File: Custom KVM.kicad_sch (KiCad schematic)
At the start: 2 parts, among them U1 TS3DV642A0RUAR, U2 TS3DV642A0RUAR

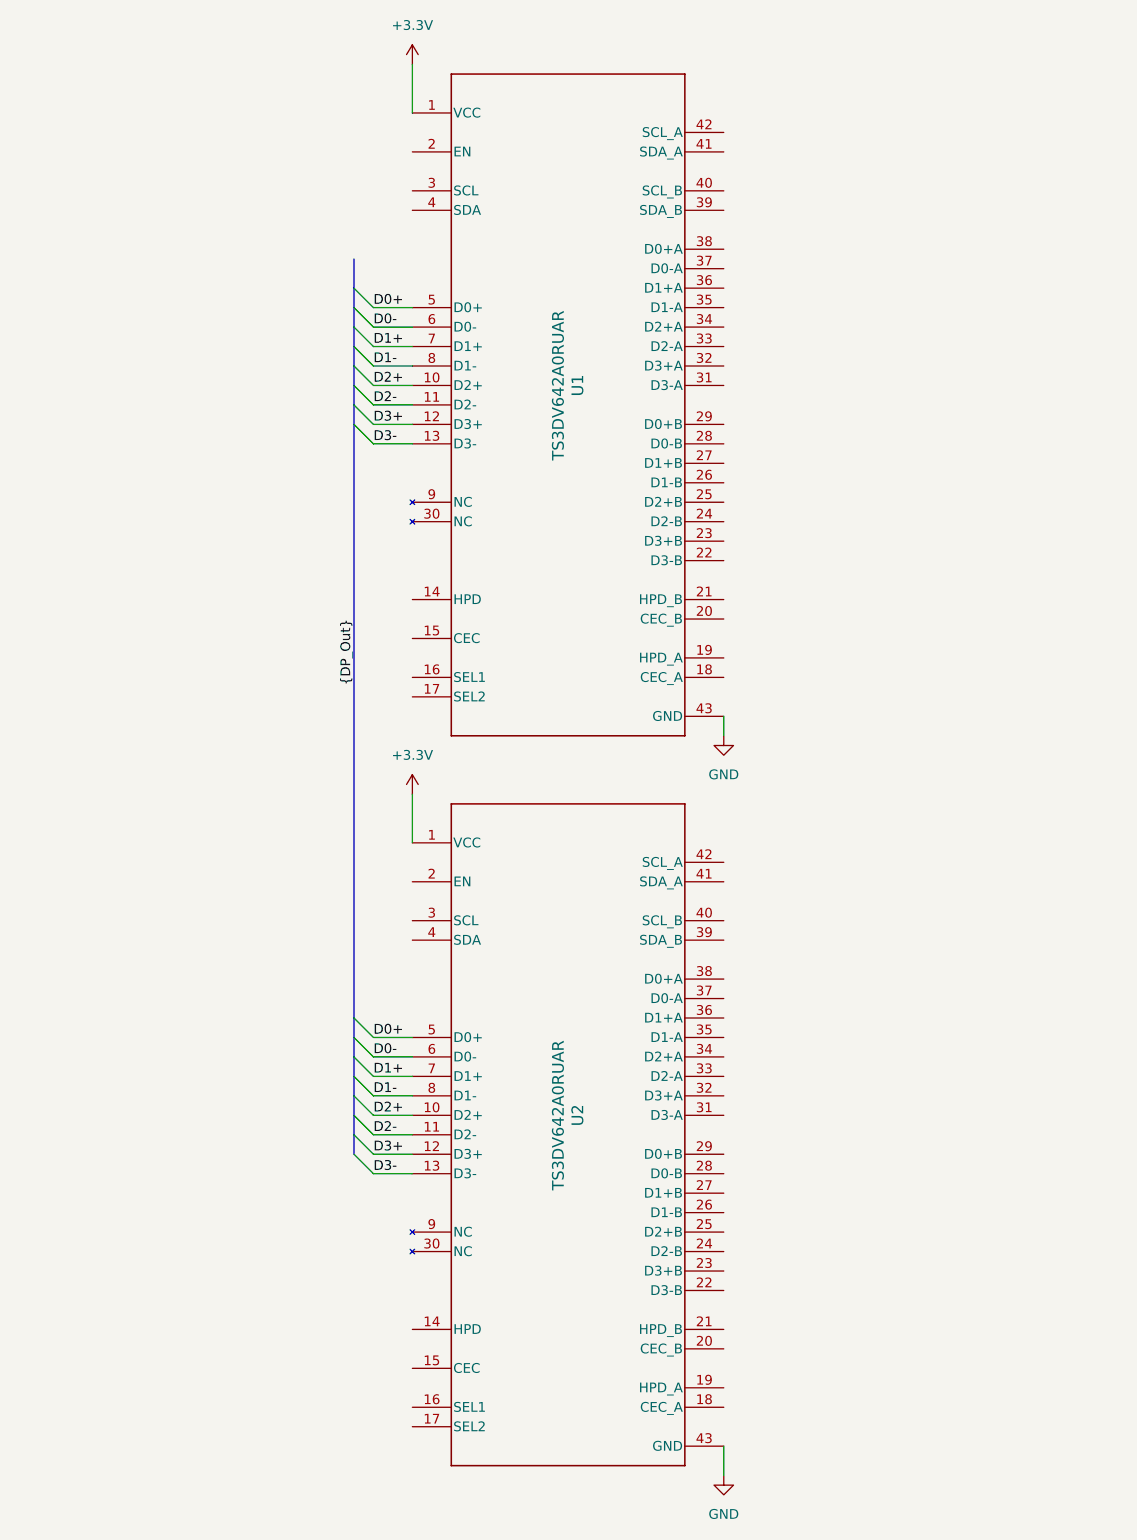
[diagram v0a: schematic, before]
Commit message: Add counter an CE circuit
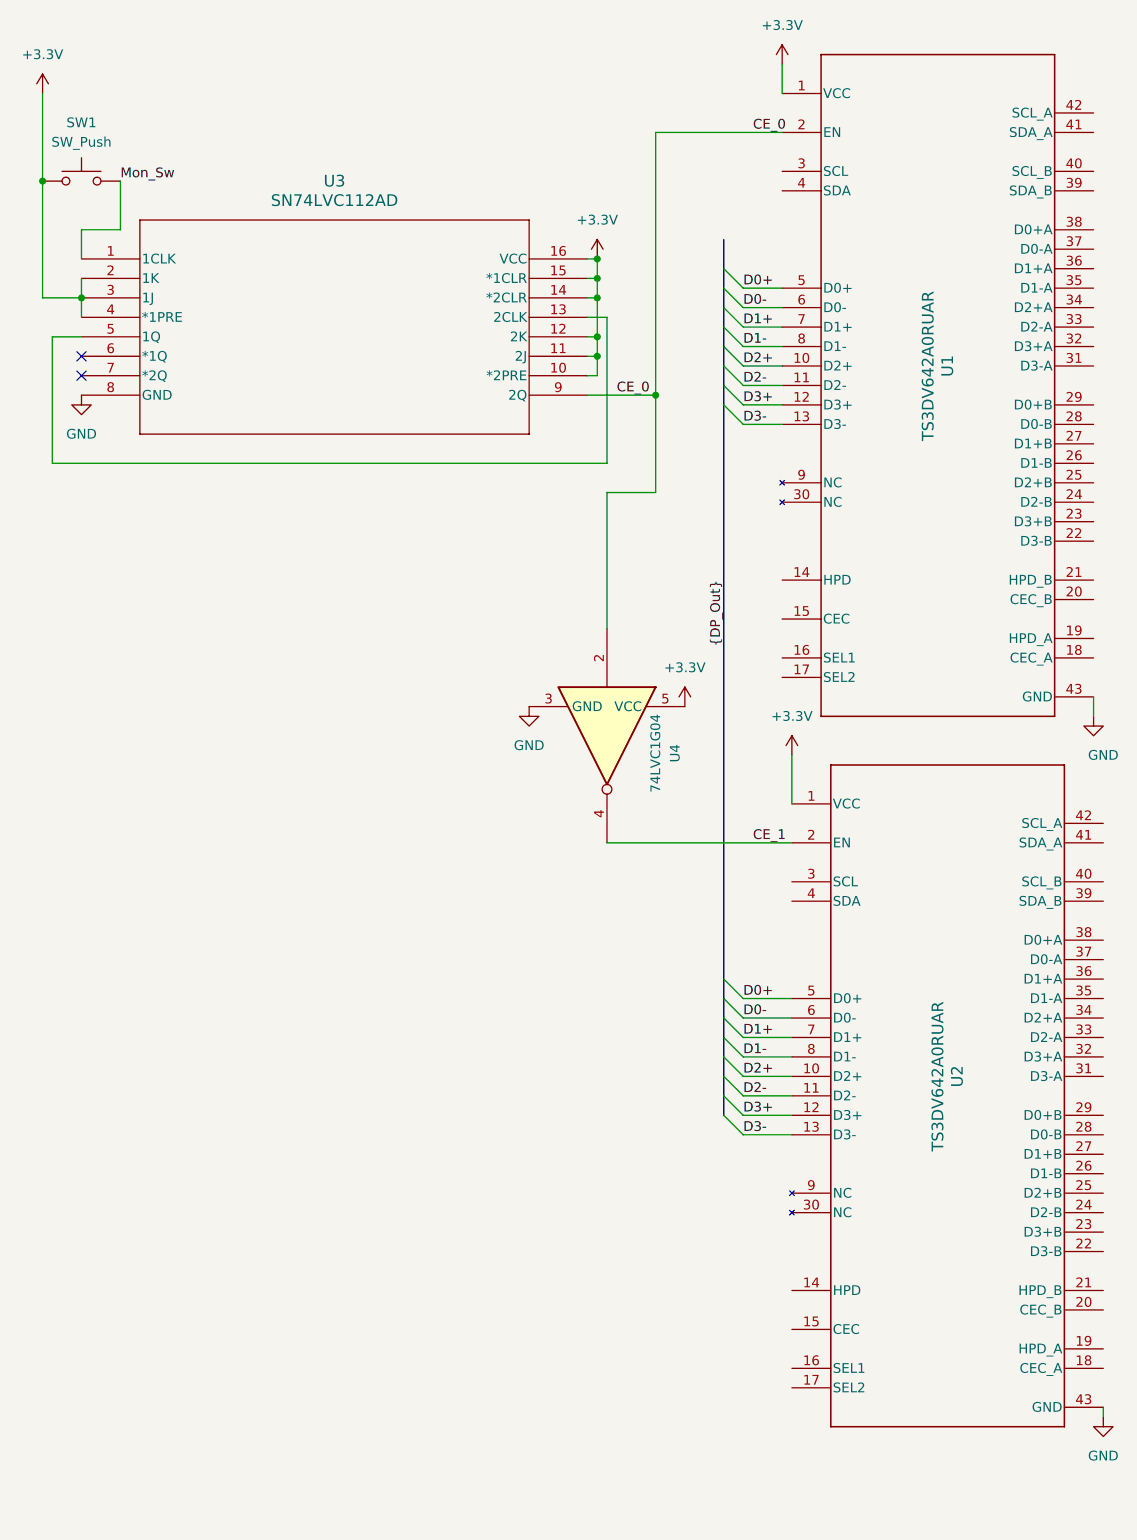
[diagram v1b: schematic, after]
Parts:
- added SW1: SW_Push, symbol Switch:SW_Push
- added U3: SN74LVC112AD, D16, symbol SN74LVC112A:SN74LVC112AD
- added U4: 74LVC1G04, symbol 74xGxx:74LVC1G04
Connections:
- net +3.3V: now also SW1.1, U3.10 (*2PRE), U3.11 (2J), U3.12 (2K), U3.14 (*2CLR), U3.15 (*1CLR), U3.16 (VCC), U3.2 (1K), U3.3 (1J), U3.4 (*1PRE), U4.5 (VCC)
- net GND: now also U3.8 (GND), U4.3 (GND)
- net CE_0: now reaches U1.2 (EN)
- net CE_0: now also U3.9 (2Q), U4.2
- net CE_1: now reaches U2.2 (EN)
- net CE_1: now also U4.4
- new net: U3.13 (2CLK), U3.5 (1Q)
- new net Mon_Sw: SW1.2, U3.1 (1CLK)
- no-connect marks 0 -> 2
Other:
- moved on the sheet: U1, U2

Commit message: Move counter and inverters to sub-sheet
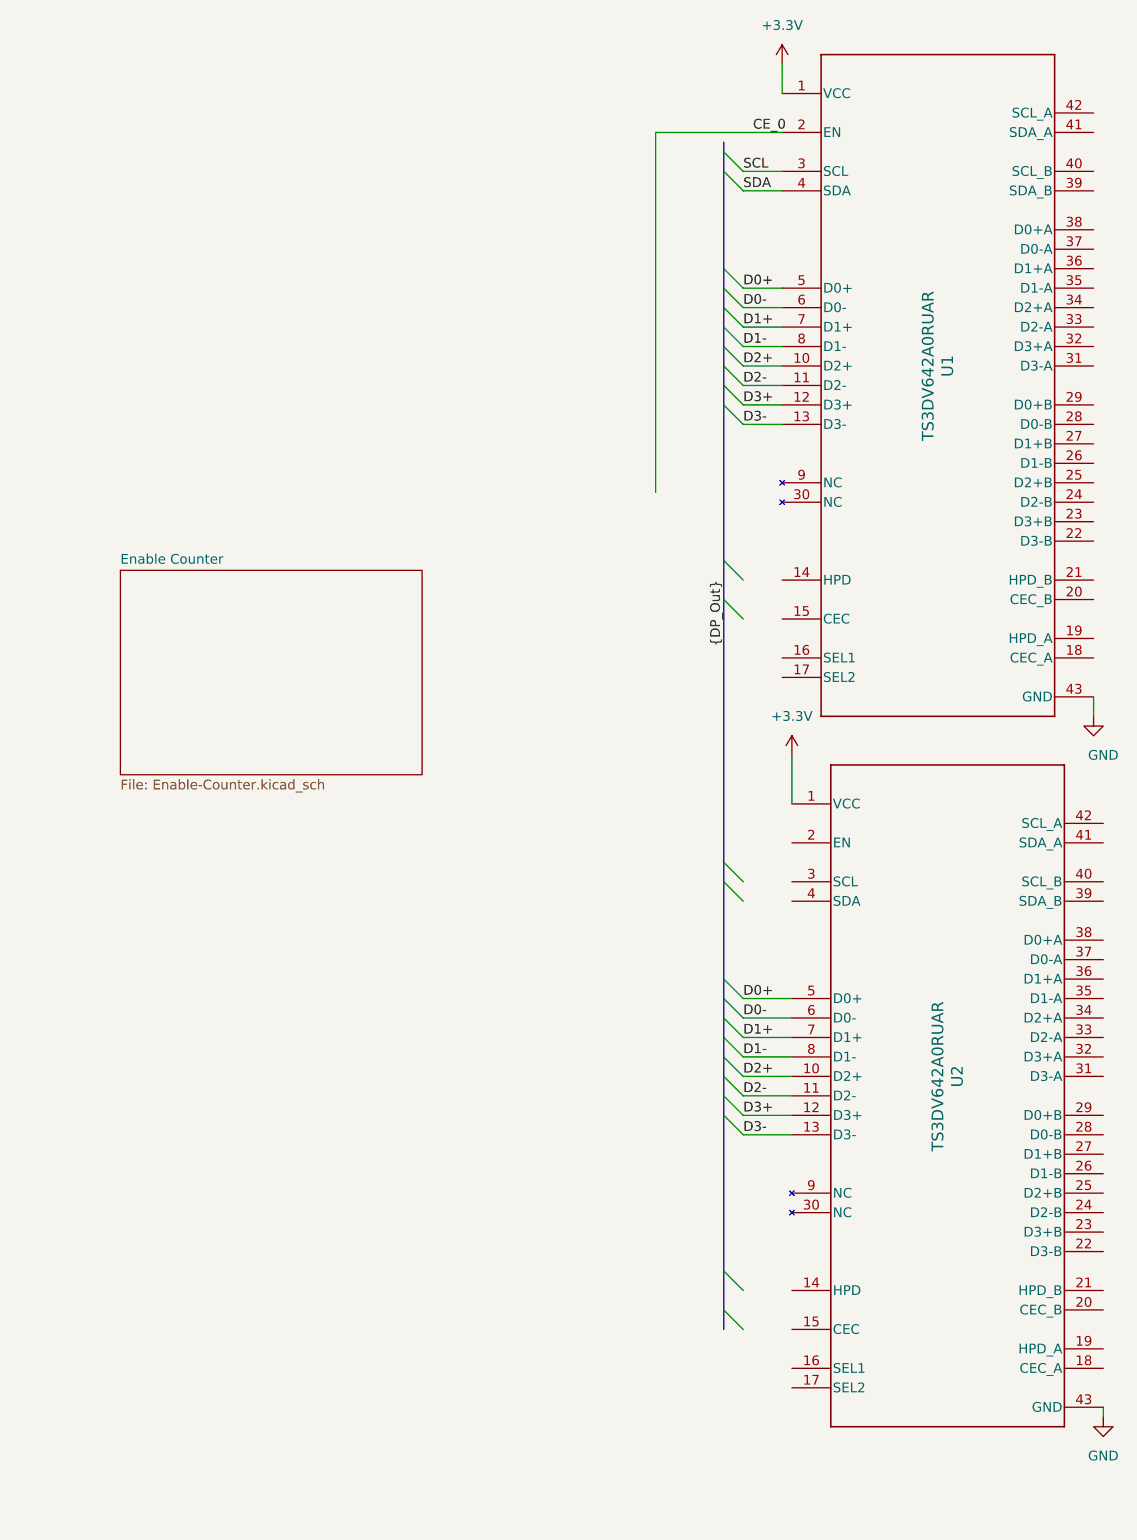
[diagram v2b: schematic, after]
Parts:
- removed SW1: SW_Push, symbol Switch:SW_Push
- removed U3: SN74LVC112AD, D16, symbol SN74LVC112A:SN74LVC112AD
- removed U4: 74LVC1G04, symbol 74xGxx:74LVC1G04
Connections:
- net SCL: now reaches U1.3 (SCL)
- net SDA: now reaches U1.4 (SDA)
- net CE_1: no longer names the net of U2.2 (EN)
- no-connect marks 2 -> 0
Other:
- added sheet Enable Counter (Enable-Counter.kicad_sch)

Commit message: Added mDP connector
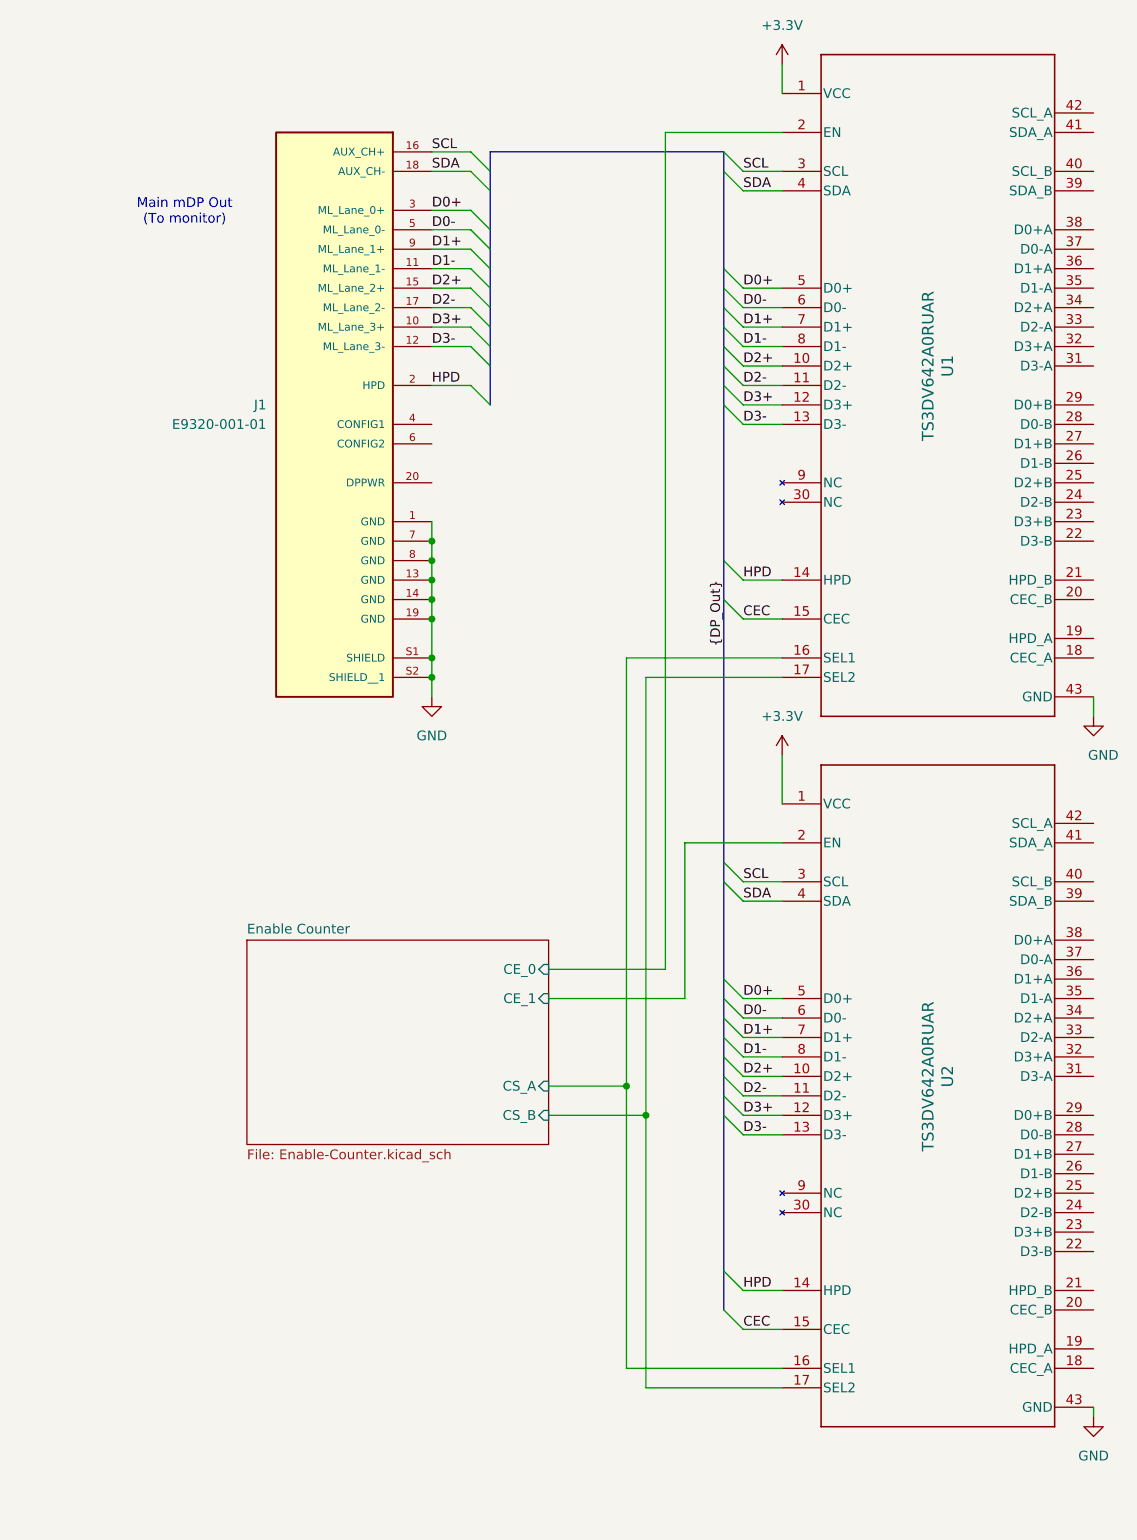
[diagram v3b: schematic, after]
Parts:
- added J1: E9320-001-01, E9320-001-01:PULSE_E9320-001-01, symbol Mini-DP:E9320-001-01
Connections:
- net D0+: now also J1.3 (ML_Lane_0+)
- net D0-: now also J1.5 (ML_Lane_0-)
- net D1+: now also J1.9 (ML_Lane_1+)
- net D1-: now also J1.11 (ML_Lane_1-)
- net D2+: now also J1.15 (ML_Lane_2+)
- net D2-: now also J1.17 (ML_Lane_2-)
- net D3+: now also J1.10 (ML_Lane_3+)
- net D3-: now also J1.12 (ML_Lane_3-)
- net GND: now also J1.1 (GND), J1.13 (GND), J1.14 (GND), J1.19 (GND), J1.7 (GND), J1.8 (GND), J1.S1 (SHIELD), J1.S2 (SHIELD__1)
- net SCL: now also U2.3 (SCL), J1.16 (AUX_CH+)
- net SDA: now also U2.4 (SDA), J1.18 (AUX_CH-)
- net HPD: now reaches U1.14 (HPD)
- net HPD: now also U2.14 (HPD), J1.2 (HPD)
- net CEC: now reaches U1.15 (CEC)
- net CEC: now also U2.15 (CEC)
- net Enable Counter/CS_A: now reaches U1.16 (SEL1)
- net Enable Counter/CS_A: now also U2.16 (SEL1)
- net Enable Counter/CS_B: now reaches U1.17 (SEL2)
- net Enable Counter/CS_B: now also U2.17 (SEL2)
- net Enable Counter/CE_1: now reaches U2.2 (EN)
- net CE_0 renamed Enable Counter/CE_0
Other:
- sheet Enable Counter ports: added CE_0, CE_1, CS_A, CS_B; removed none
- note added: "Main mDP Out (To monitor)"
- moved on the sheet: U2

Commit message: Add Switching subsheet
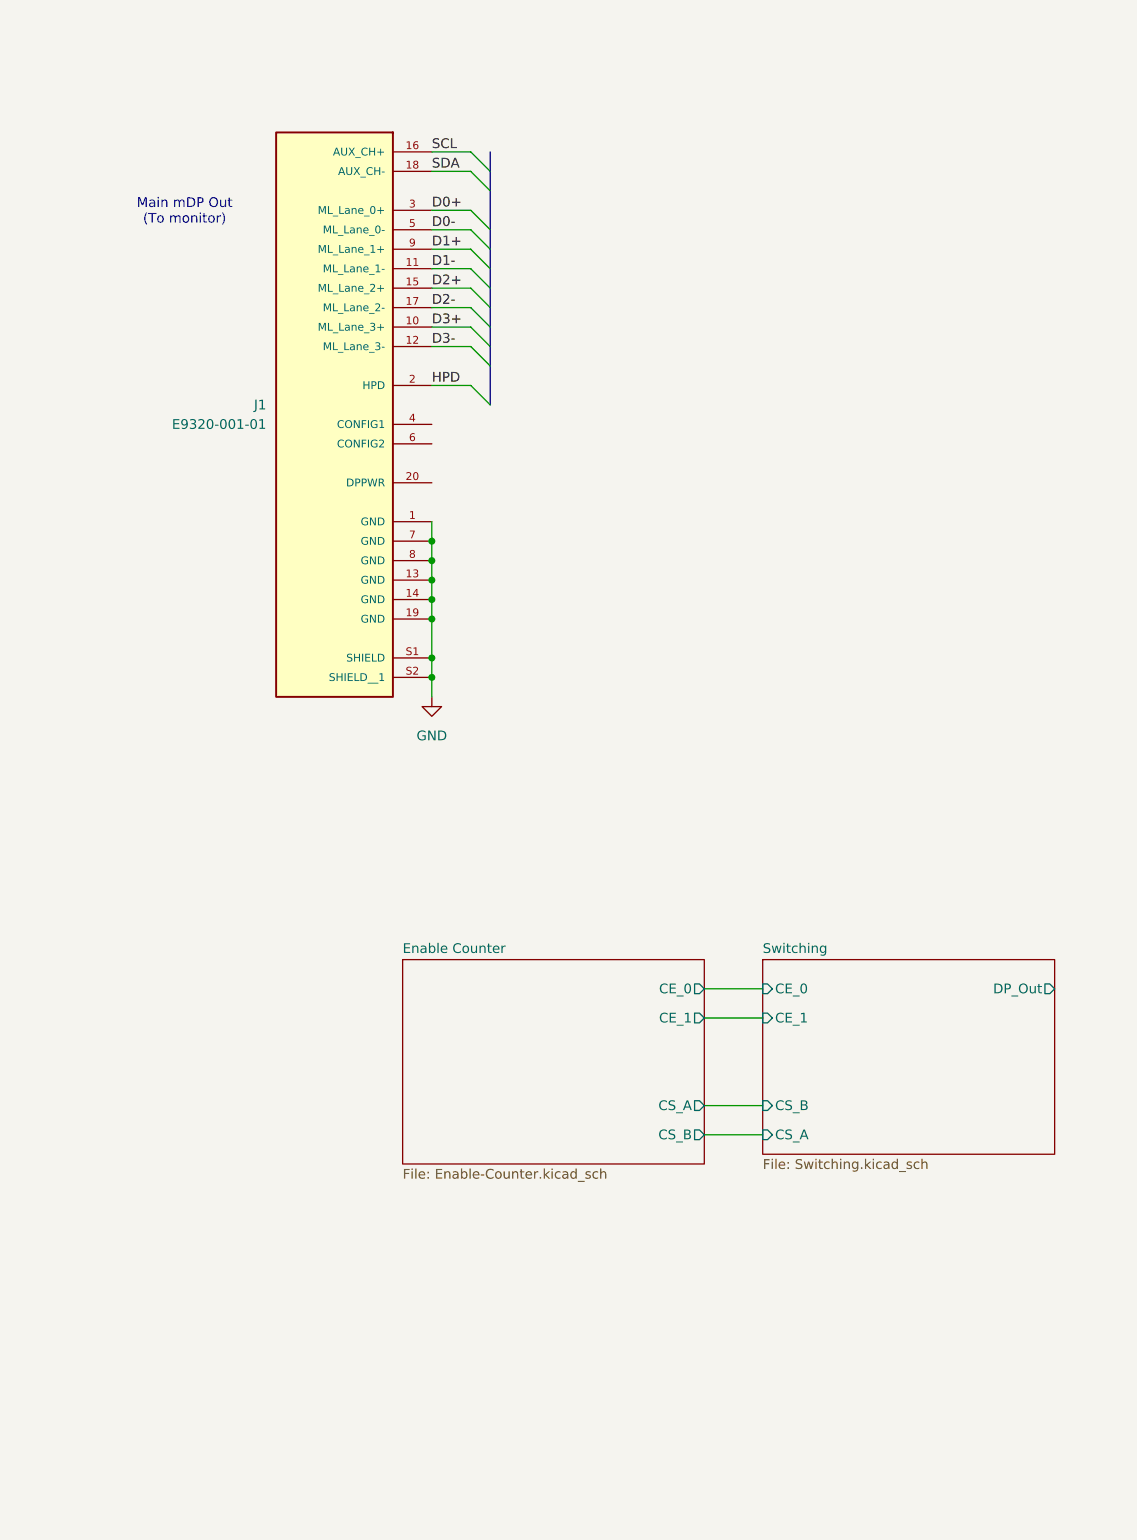
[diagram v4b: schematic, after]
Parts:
- removed U1, U2: TS3DV642A0RUAR, RUA0042A, symbol TS3DV642:TS3DV642A0RUAR
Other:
- added sheet Switching (Switching.kicad_sch)
